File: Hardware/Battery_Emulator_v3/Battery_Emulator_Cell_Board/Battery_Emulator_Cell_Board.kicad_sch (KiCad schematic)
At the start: 45 parts, among them J3 Cell1_Vout, J4 Conn_01x05, Q1 IRFB7545PBF, Q2 MJE2955T, Q3 MJE2955T, U1 LT3080xQ, U2 ISO1640BDR, U3 MCP4651T-103E_ST, U4 KA78M05_TO252, U5 MCP6001UT-I/OT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

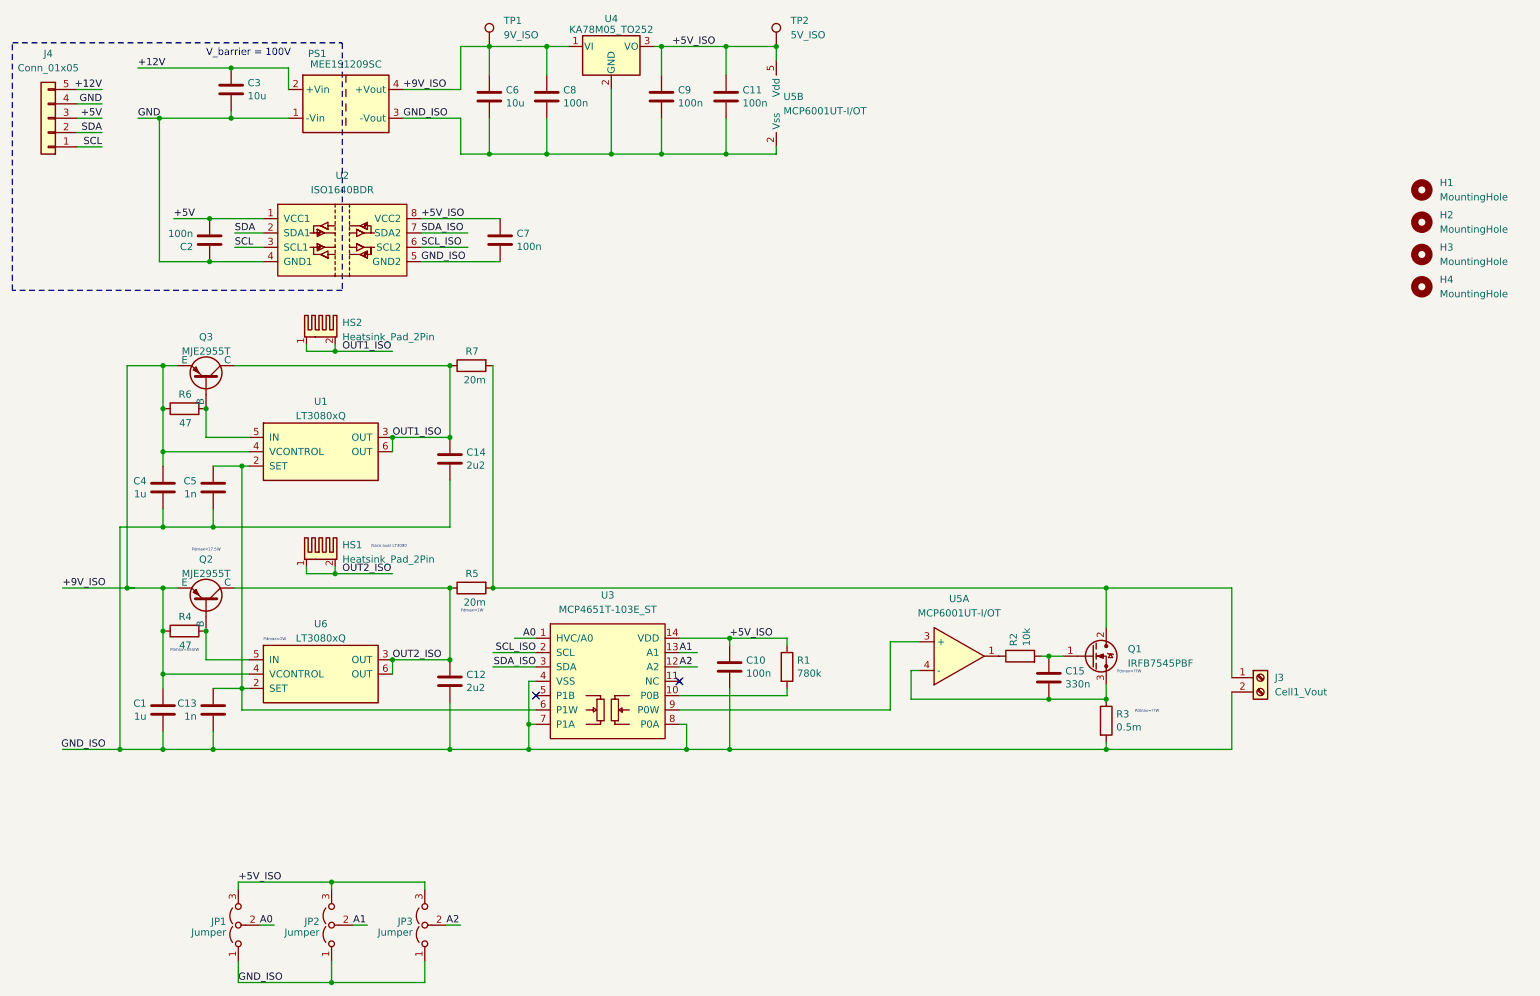
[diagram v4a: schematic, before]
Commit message: Hardware Update
Updated the layout of the cell board PCB
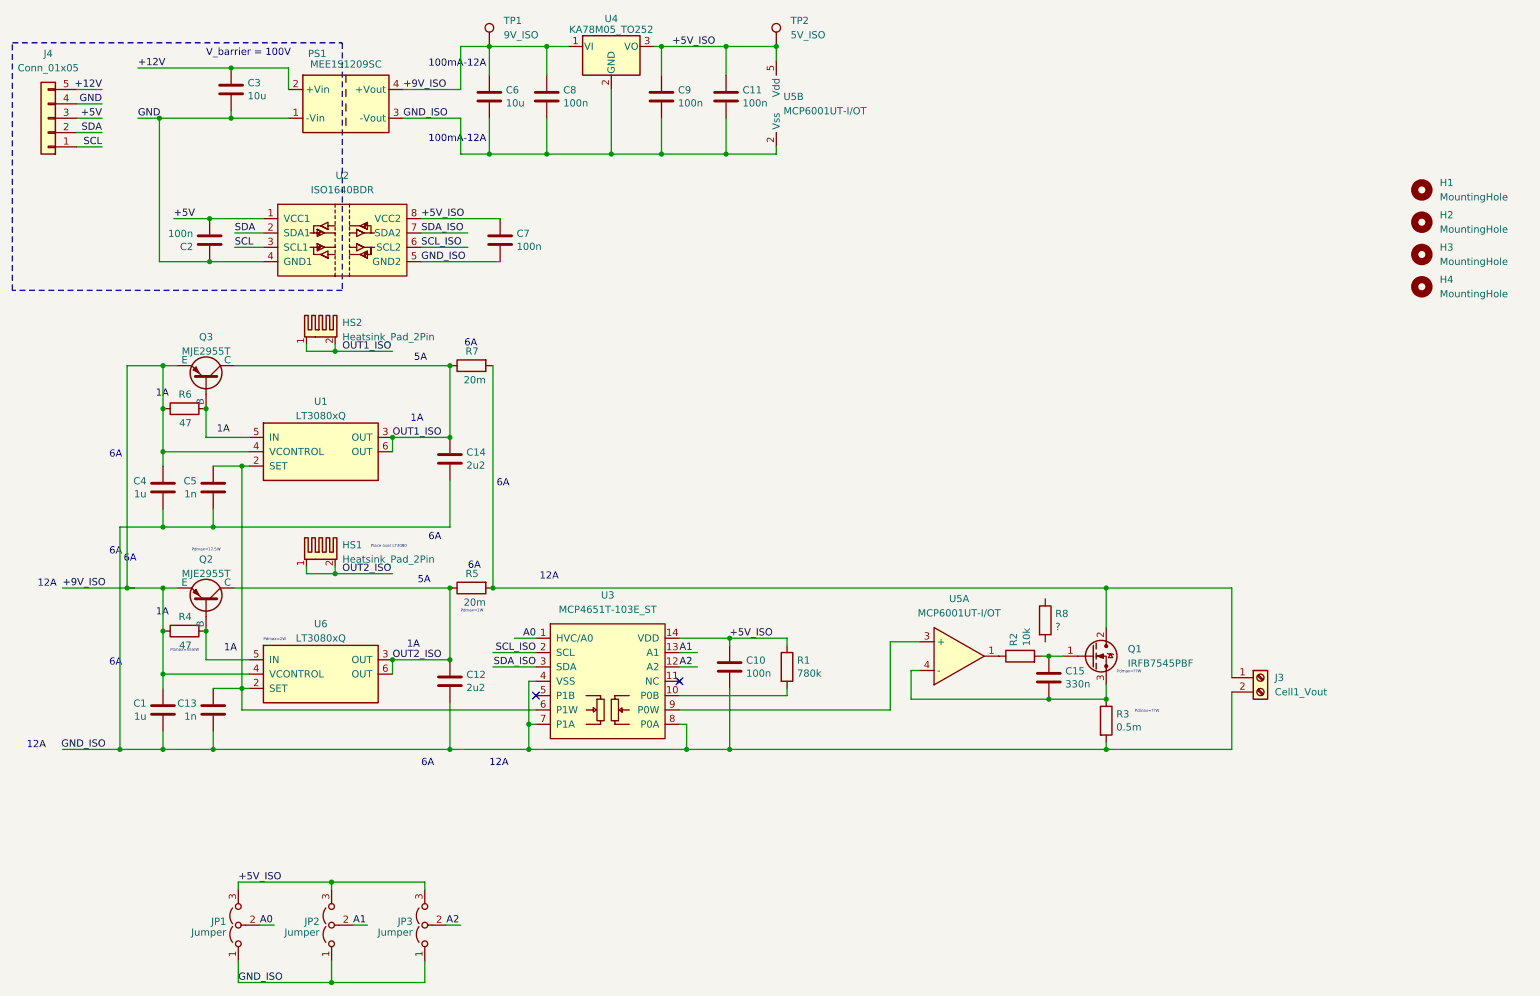
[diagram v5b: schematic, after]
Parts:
- added R8: ?, Resistor_SMD:R_0805_2012Metric, symbol Device:R
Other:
- note added: "100mA-12A"
- note added: "12A"
- note added: "1A"
- note added: "5A"
- note added: "6A"
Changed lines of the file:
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@@
     (fill (type none))
   )
+  (text "12A" (at 108.585 113.665 0)
+    (effects (font (size 1.27 1.27) (color 255 0 255 1)) (justify left bottom))
+  )
   (text "Pdmax=1W" (at 94.615 119.38 0)
     (effects (font (size 0.5 0.5)) (justify left bottom))
   )
+  (text "12A" (at 99.695 146.685 0)
+    (effects (font (size 1.27 1.27) (color 255 0 255 1)) (justify left bottom))
+  )
+  (text "1A" (at 40.64 81.28 0)
+    (effects (font (size 1.27 1.27) (color 255 0 255 1)) (justify left bottom))
+  )
   (text "Pdmax=55mW" (at 43.18 126.365 0)
     (effects (font (size 0.5 0.5)) (justify left bottom))
   )
+  (text "12A" (at 19.685 114.935 0)
+    (effects (font (size 1.27 1.27) (color 255 0 255 1)) (justify left bottom))
+  )
+  (text "6A" (at 88.9 106.68 0)
+    (effects (font (size 1.27 1.27) (color 255 0 255 1)) (justify left bottom))
+  )
+  (text "5A" (at 86.36 74.93 0)
+    (effects (font (size 1.27 1.27) (color 255 0 255 1)) (justify left bottom))
+  )
+  (text "6A" (at 32.385 109.22 0)
+    (effects (font (size 1.27 1.27) (color 255 0 255 1)) (justify left bottom))
+  )
+  (text "6A" (at 34.925 110.49 0)
+    (effects (font (size 1.27 1.27) (color 255 0 255 1)) (justify left bottom))
+  )
   (text "Place over LT3080" (at 78.74 107.95 0)
     (effects (font (size 0.5 0.5)) (justify left bottom))
   )
+  (text "1A" (at 51.435 87.63 0)
+    (effects (font (size 1.27 1.27) (color 255 0 255 1)) (justify left bottom))
+  )
+  (text "1A" (at 85.09 125.73 0)
+    (effects (font (size 1.27 1.27) (color 255 0 255 1)) (justify left bottom))
+  )
+  (text "5A" (at 86.995 114.3 0)
+    (effects (font (size 1.27 1.27) (color 255 0 255 1)) (justify left bottom))
+  )
+  (text "6A" (at 100.965 97.155 0)
+    (effects (font (size 1.27 1.27) (color 255 0 255 1)) (justify left bottom))
+  )
   (text "Pdmax=??W" (at 210.82 130.175 0)
     (effects (font (size 0.5 0.5)) (justify left bottom))
+  )
+  (text "6A" (at 32.385 128.905 0)
+    (effects (font (size 1.27 1.27) (color 255 0 255 1)) (justify left bottom))
+  )
+  (text "1A" (at 52.705 126.365 0)
+    (effects (font (size 1.27 1.27) (color 255 0 255 1)) (justify left bottom))
+  )
+  (text "100mA-12A" (at 88.9 22.86 0)
+    (effects (font (size 1.27 1.27) (color 255 0 255 1)) (justify left bottom))
   )
   (text "V_barrier = 100V" (at 49.53 20.955 0)
     (effects (font (size 1.27 1.27) (color 255 0 0 1)) (justify left bottom))
   )
+  (text "6A" (at 95.25 72.39 0)
+    (effects (font (size 1.27 1.27) (color 255 0 255 1)) (justify left bottom))
+  )
+  (text "100mA-12A" (at 88.9 36.195 0)
+    (effects (font (size 1.27 1.27) (color 255 0 255 1)) (justify left bottom))
+  )
   (text "Pdmax=17.5W" (at 46.99 108.585 0)
     (effects (font (size 0.5 0.5)) (justify left bottom))
   )
+  (text "6A" (at 87.63 146.685 0)
+    (effects (font (size 1.27 1.27) (color 255 0 255 1)) (justify left bottom))
+  )
+  (text "1A" (at 40.64 120.015 0)
+    (effects (font (size 1.27 1.27) (color 255 0 255 1)) (justify left bottom))
+  )
+  (text "6A" (at 32.385 92.075 0)
+    (effects (font (size 1.27 1.27) (color 255 0 255 1)) (justify left bottom))
+  )
   (text "Pdmax=2W" (at 59.69 124.46 0)
     (effects (font (size 0.5 0.5)) (justify left bottom))
   )
+  (text "6A" (at 95.885 111.76 0)
+    (effects (font (size 1.27 1.27) (color 255 0 255 1)) (justify left bottom))
+  )
+  (text "12A" (at 17.78 143.51 0)
+    (effects (font (size 1.27 1.27) (color 255 0 255 1)) (justify left bottom))
+  )
+  (text "1A" (at 85.725 85.725 0)
+    (effects (font (size 1.27 1.27) (color 255 0 255 1)) (justify left bottom))
+  )
   (text "Pdmax=??W" (at 213.995 137.16 0)
     (effects (font (size 0.5 0.5)) (justify left bottom))
@@
     (effects (font (size 1.27 1.27)) (justify right bottom))
   )
+  (symbol (lib_id "Device:R") (at 198.12 120.65 0) (unit 1)
+    (in_bom yes) (on_board yes) (dnp no)
+    (property "Reference" "R8" (at 199.898 119.4816 0)
+      (effects (font (size 1.27 1.27)) (justify left))
+    )
+    (property "Value" "?" (at 199.898 121.793 0)
+      (effects (font (size 1.27 1.27)) (justify left))
+    )
+    (property "Footprint" "Resistor_SMD:R_0805_2012Metric" (at 196.342 120.65 90)
+      (effects (font (size 1.27 1.27)) hide)
+    )
+    (property "Datasheet" "~" (at 198.12 120.65 0)
+      (effects (font (size 1.27 1.27)) hide)
+    )
+    (pin "1")
+    (pin "2")
+    (instances
+      (project "Battery_Emulator_Cell_Board"
+        (path "/180aea6f-6c78-4f59-bff6-104a9c25165d"
+          (reference "R8") (unit 1)
+        )
+      )
+      (project "Battery_Emulator"
+        (path "/bb7641ff-0dfd-4f4a-b3be-57afbbb9fdac"
+          (reference "R?") (unit 1)
+        )
+        (path "/bb7641ff-0dfd-4f4a-b3be-57afbbb9fdac/86a0f187-fc20-4f8c-b621-2752c8234446"
+          (reference "R1") (unit 1)
+        )
+        (path "/bb7641ff-0dfd-4f4a-b3be-57afbbb9fdac/b6a9662d-5d6a-45a2-997c-bd44d3cd27c8"
+          (reference "R8") (unit 1)
+        )
+        (path "/bb7641ff-0dfd-4f4a-b3be-57afbbb9fdac/9e64a729-6adc-46a2-82ae-c445b486d477"
+          (reference "R11") (unit 1)
+        )
+        (path "/bb7641ff-0dfd-4f4a-b3be-57afbbb9fdac/c6b7f9ee-0ac8-4ec0-aa5c-5805ca169953"
+          (reference "R14") (unit 1)
+        )
+      )
+    )
+  )
   (symbol (lib_id "Connector:TestPoint") (at 99.695 19.05 0) (unit 1)

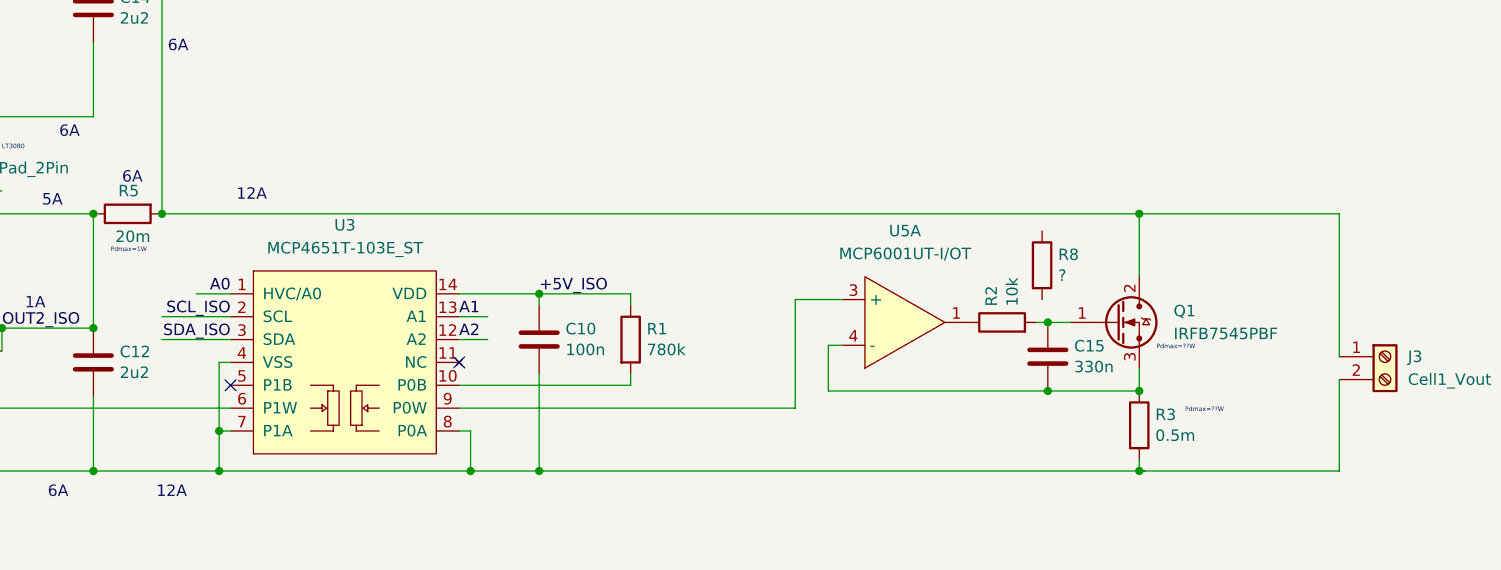
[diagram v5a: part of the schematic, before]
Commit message: added current sink resistor
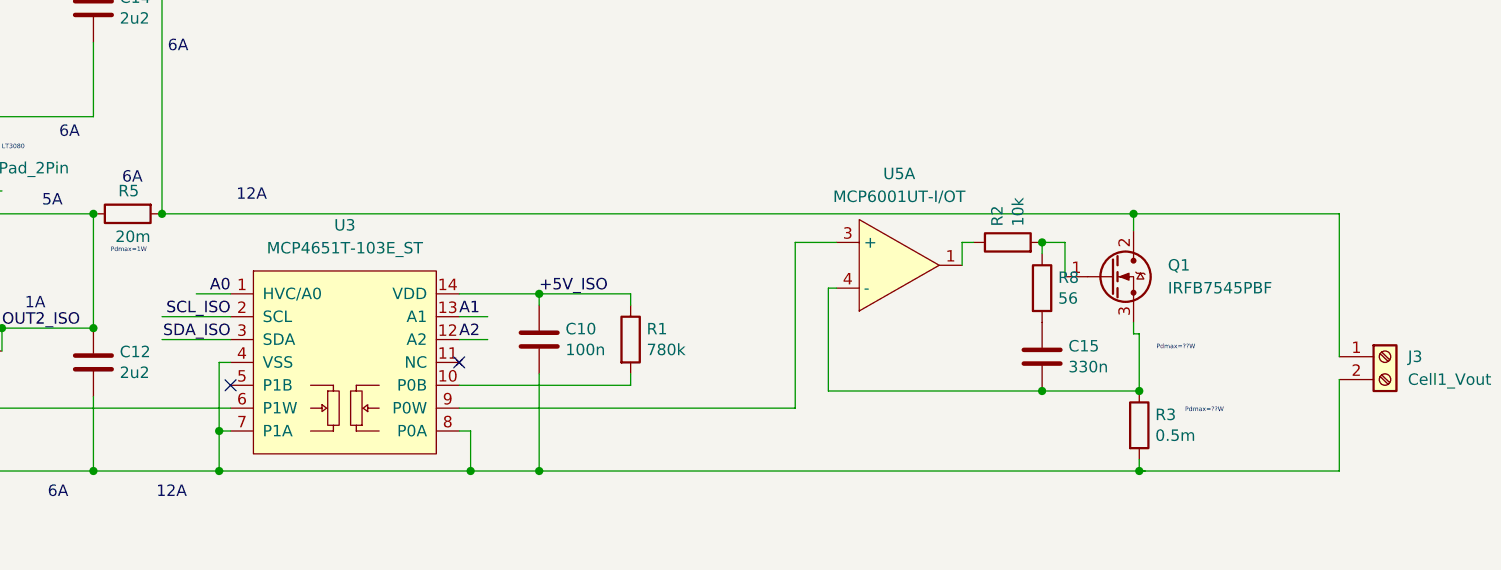
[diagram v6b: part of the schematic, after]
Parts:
- R8: value ? -> 56
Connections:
- net at R8.1: now also Q1.1, R2.2
- net at R8.2: now also C15.1
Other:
- moved on the sheet: C15, Q1, R2, R8, U5A
